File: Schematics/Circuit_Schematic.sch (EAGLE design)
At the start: 33 parts, among them Q1 L7812ACV, U1 TDA2822M, X1 1502_01

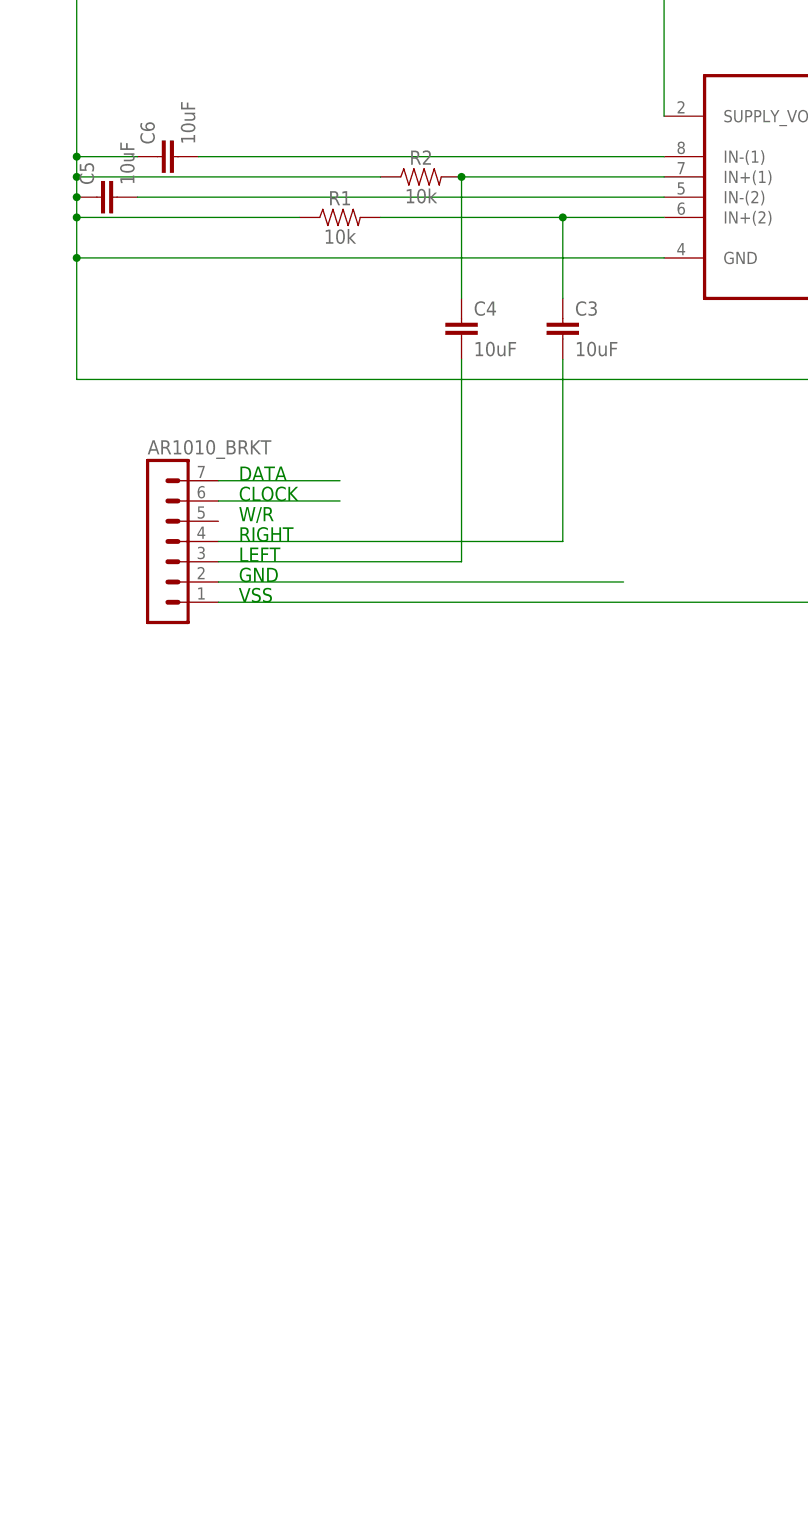
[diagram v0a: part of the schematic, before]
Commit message: added esp8266-12e and pots for volume adjust on amp
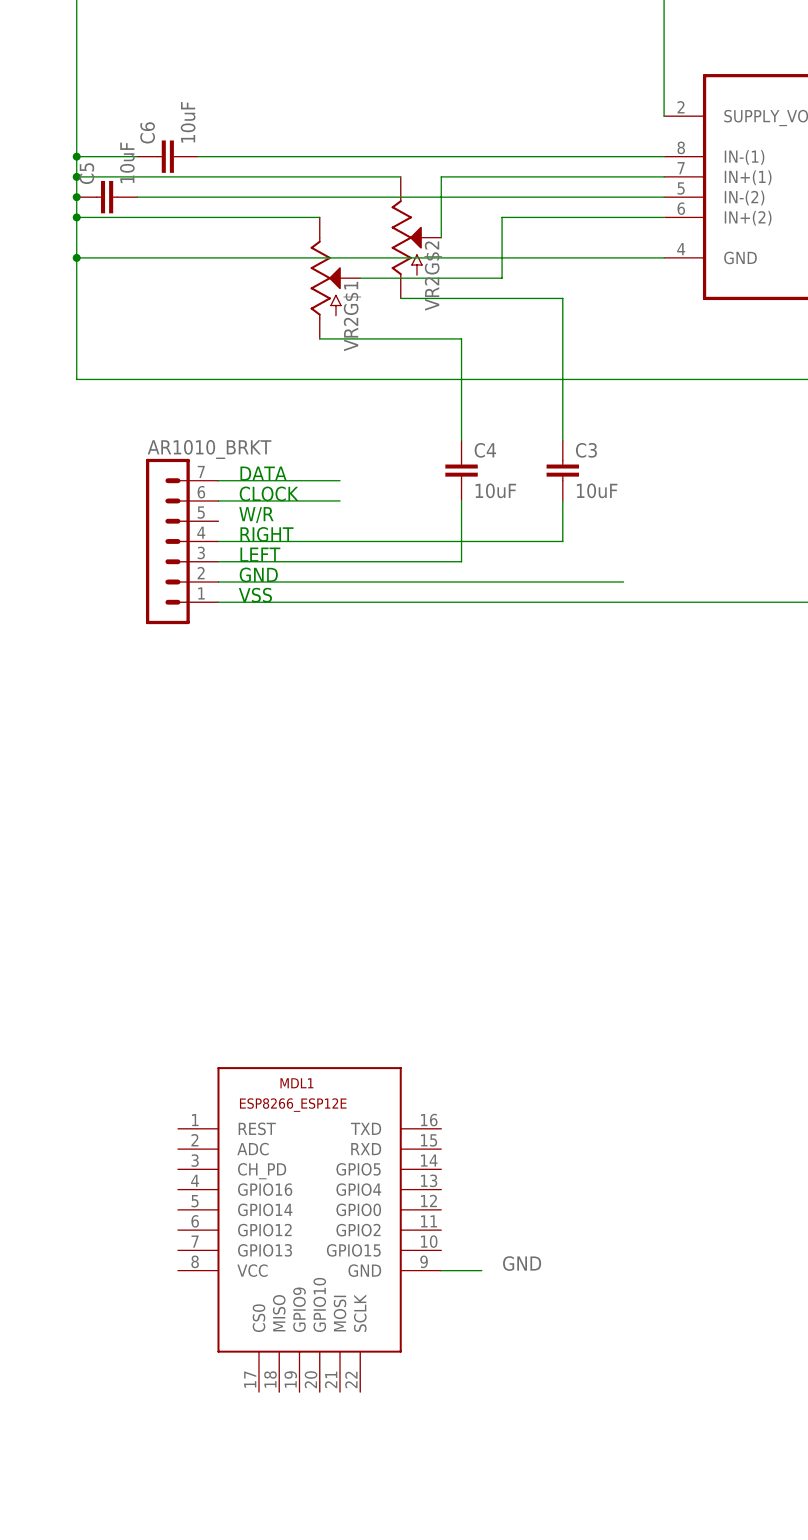
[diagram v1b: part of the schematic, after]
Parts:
- removed R1, R2: 10k, SparkFun-Resistors:10KOHM-0603-1/10W-1%
- added MDL1: (no value), ESP8266-12E:ESP8266-12EESP8266-ESP12E
- added VR2: (no value), SparkFun-Resistors:POTENTIOMETER_DUAL-PTH-12MM-1/20W-20%
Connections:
- new net N$4: U1.IN+(1), VR2G$2.S
- new net N$5: U1.IN+(2), VR2G$1.S
- net GND: now also MDL1.GND, VR2G$1.E, VR2G$2.E; no longer R1.1, R2.1
- net N$11: now also VR2G$1.A; no longer R2.2, U1.IN+(1)
- net N$12: now also VR2G$2.A; no longer R1.2, U1.IN+(2)
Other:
- moved on the sheet: C3, C4

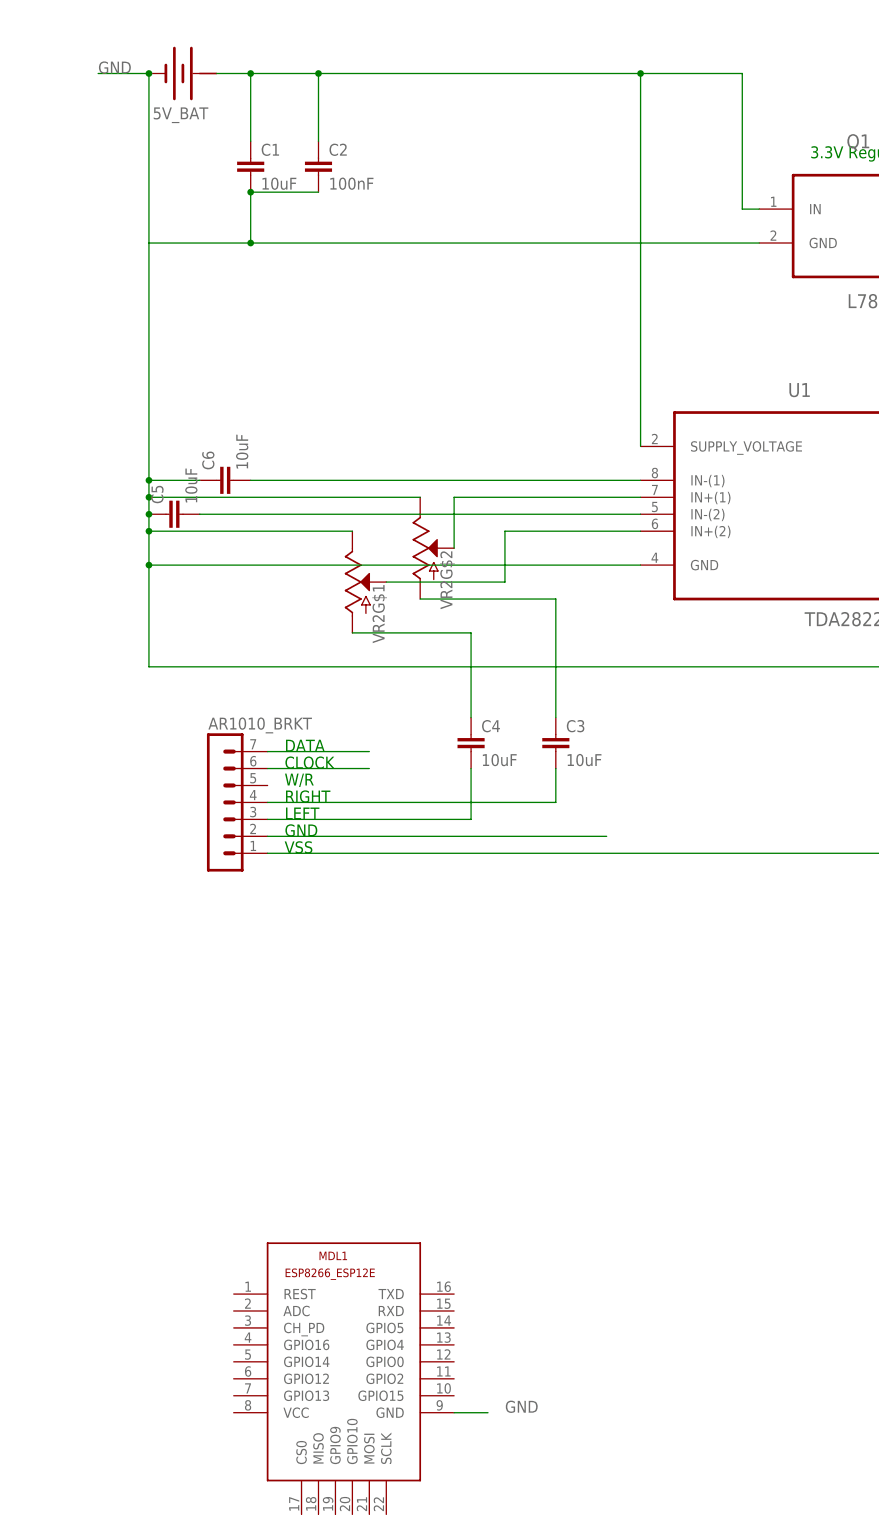
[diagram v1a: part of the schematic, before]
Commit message: updated schematic to include switch and led
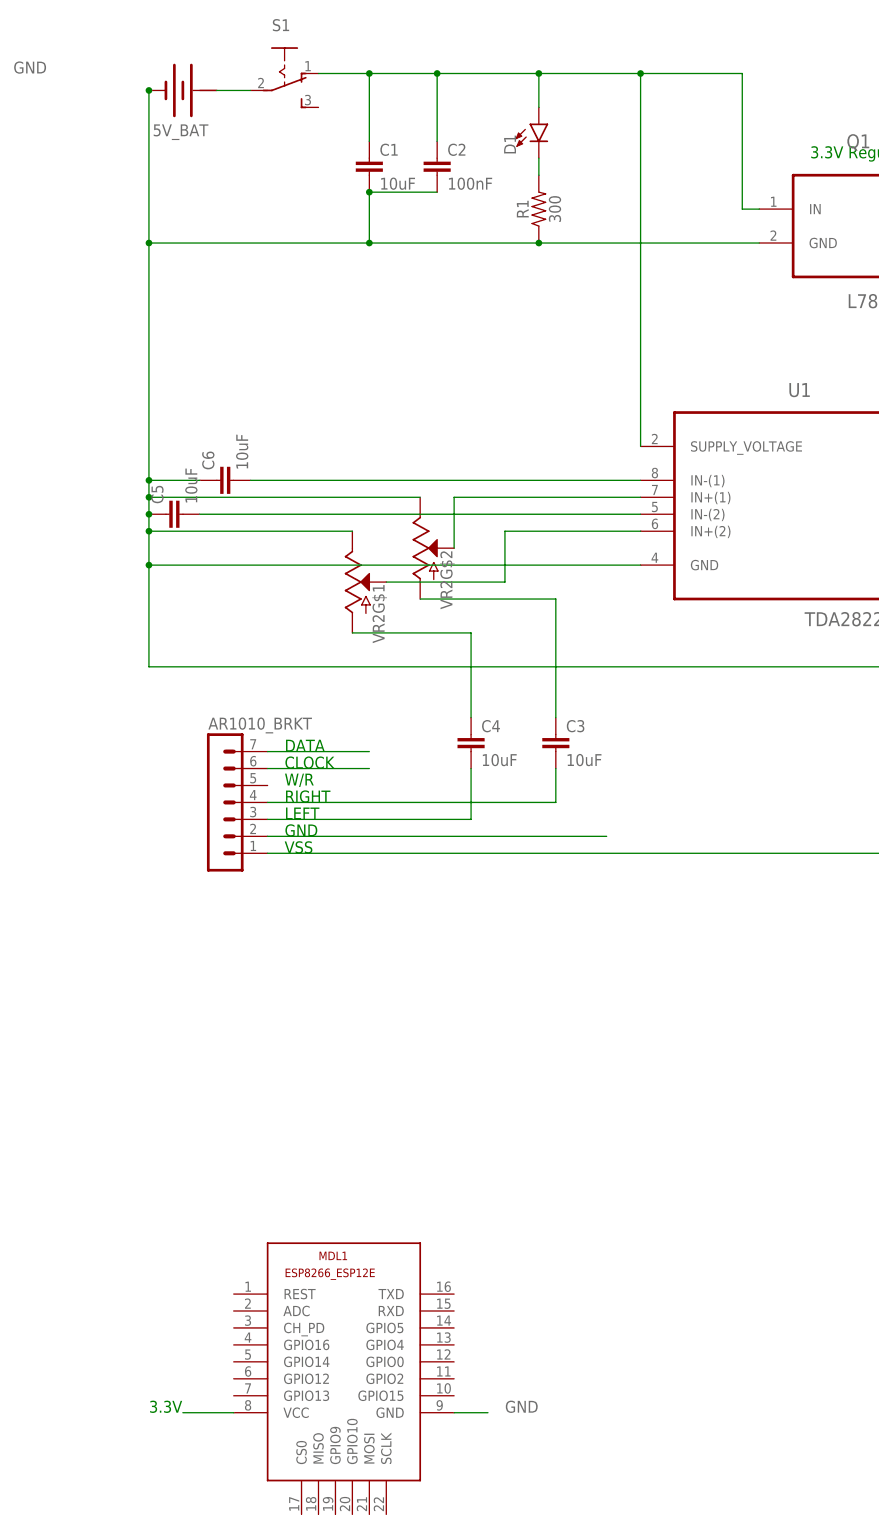
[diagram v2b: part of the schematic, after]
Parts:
- added D1: (no value), SparkFun-LED:LED10MM
- added R1: 300, SparkFun-Resistors:1OHM-0603-1/10W-1%
- added S1: (no value), switch:255SB
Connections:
- removed net N$32: C1.2, C2.2, Q1.GND
- new net N$18: D1.C, R1.2
- new net N$20: 5V_BAT.+, S1.P
- new net N$21: MDL1.VCC
- net GND: now also C1.2, C2.2, Q1.GND, R1.1
- net VDD: now also D1.A, S1.O; no longer 5V_BAT.+
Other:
- note added: "3.3V"
- moved on the sheet: 5V_BAT, C1, C2
